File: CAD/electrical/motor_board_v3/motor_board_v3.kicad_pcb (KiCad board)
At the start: 4 copper layers, 62 x 34 mm, 82 parts, among them J1 Conn_ST_STDC14, J2 12V, J3 I2C, J4 RS485, J5 Stepper, J6 Stepper, J7 Stepper, Q1 SI2301CDS-T1-GE3, U1 STM32F401RCTx, U2 MAX485E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

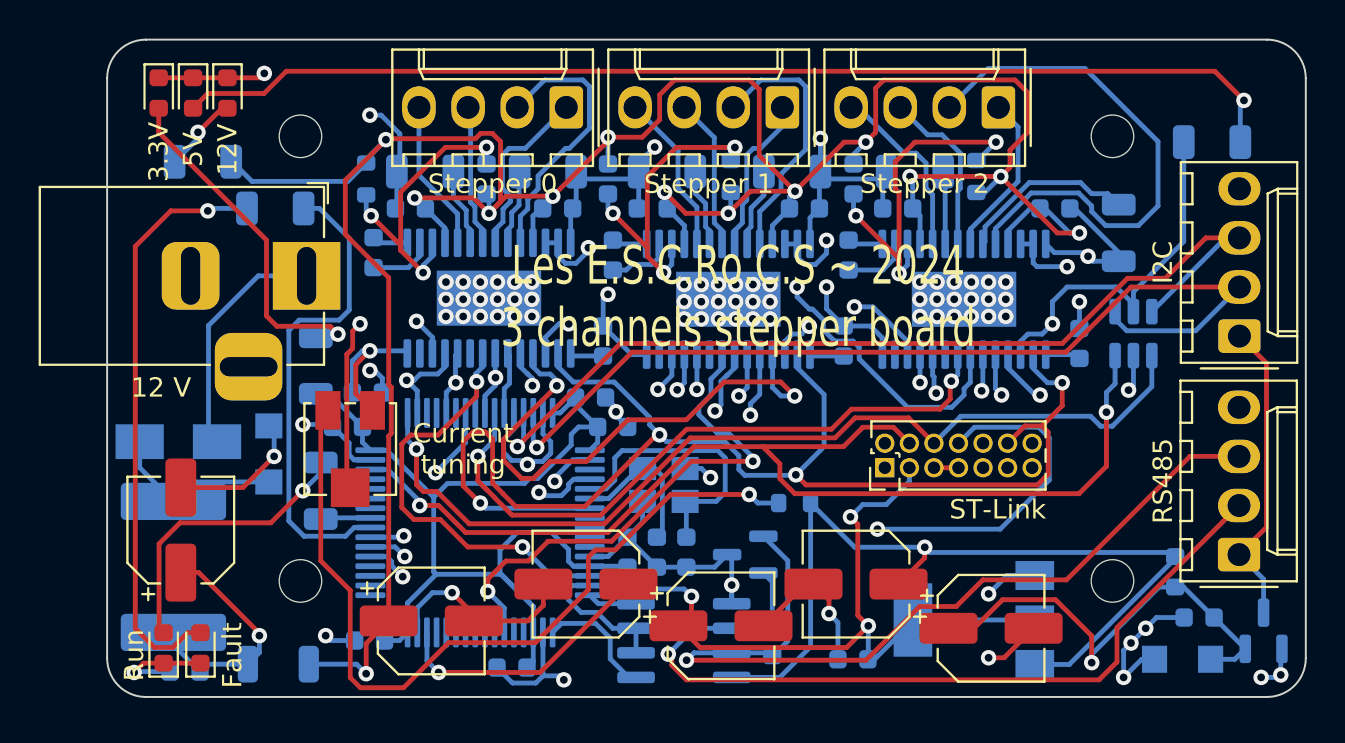
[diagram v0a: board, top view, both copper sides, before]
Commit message: Updated version of motor board and main board (#3)
* Cleaning backup files

* [WIP] Main board V2

* [WIP] Implement RS485 in ultrasonic board

* Updated version of motor board and main board
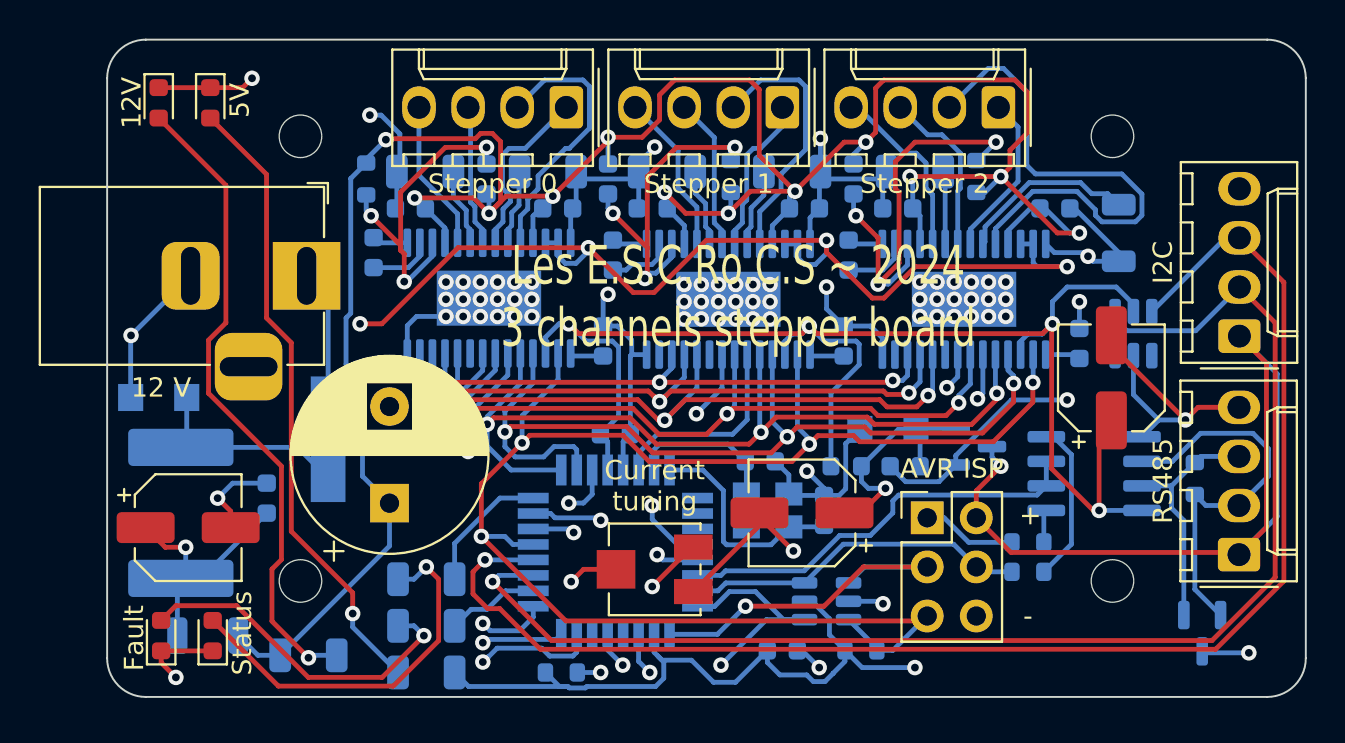
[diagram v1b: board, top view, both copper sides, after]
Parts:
- removed C23, C25, C26, C27, C28, C33: 100n, Capacitor_SMD:C_0603_1608Metric
- removed C29: 4.7u, Capacitor_SMD:CP_Elec_5x5.4
- removed C32: 10u, Capacitor_SMD:CP_Elec_5x5.4
- removed D4: 3V3, LED_SMD:LED_0603_1608Metric
- removed R8: 470, Resistor_SMD:R_1206_3216Metric
- added R19: 10k, Resistor_SMD:R_0603_1608Metric, B.Cu at (170.6, 110.7)
- added R2: 330, Resistor_SMD:R_0603_1608Metric, B.Cu at (179.2, 106.7)
- added R3: 330, Resistor_SMD:R_0603_1608Metric, B.Cu at (179.2, 105.2)
- C1, C2: value 22p -> 100n
- C11, C17: value 100n -> 22p
- C30: footprint Capacitor_SMD:CP_Elec_5x5.4 -> Capacitor_THT:CP_Radial_D10.0mm_P5.00mm
- J1: value Conn_ST_STDC14 -> AVR-ISP-6; footprint Connector_PinHeader_1.27mm:PinHeader_2x07_P1.27mm_Vertical -> Connector_PinHeader_2.54mm:PinHeader_2x03_P2.54mm_Vertical
- U1: value STM32F401RCTx -> ATmega328PB-A; footprint Package_QFP:LQFP-64_10x10mm_P0.5mm -> Package_QFP:TQFP-32_7x7mm_P0.8mm
- U6: value AMS1117-3.3 -> SRV05-4; footprint Package_TO_SOT_SMD:SOT-223-3_TabPin2 -> Package_TO_SOT_SMD:SOT-23-6
- Y1: value 25MHz -> 16MHz
- moved R7 49.0 mm to (148.1, 111.9), turned to 180 degrees
- moved R1 26.1 mm to (142.0, 111.0), turned to 0 degrees
- moved D9 24.0 mm to (188.2, 109.9), turned to -90 degrees
- moved R5 23.4 mm to (187.8, 101.9), turned to -90 degrees
- moved R4 23.0 mm to (148.1, 109.5)
- moved U2 22.9 mm to (182.6, 101.6)
- moved C11 20.6 mm to (165.4, 101.0), turned to 0 degrees
- moved D7 19.3 mm to (172.0, 99.3)
- moved FB2 17.9 mm to (169.8, 101.2), turned to 180 degrees
- moved Q1 17.8 mm to (176.4, 100.2), turned to 0 degrees
- moved C4 17.1 mm to (172.8, 101.2)
- moved C31 17.0 mm to (183.5, 96.6), turned to 90 degrees
- moved RV1 16.9 mm to (159.9, 106.6), turned to -90 degrees
- moved R18 14.9 mm to (155.1, 111.9), turned to 0 degrees
- moved C3 11.5 mm to (167.5, 103.6), turned to 180 degrees
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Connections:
- C1 pad 1: /XTAL1 -> +5V
- C11 pad 1: /RST -> /XTAL1
- C17 pad 1: +3V3 -> /XTAL2
- C2 pad 1: /XTAL2 -> +5V
- J1 pad 1: unconnected-(J1-Pad1) -> /SPI_MISO
- J1 pad 2: unconnected-(J1-Pad2) -> /RAW_5V
- J1 pad 3: +3V3 -> /SPI_SCK
- J1 pad 4: /SWDIO -> /SPI_MOSI
- J1 pad 5: GND -> /RST
- J1 pad 6: /SWCLK -> GND
- U1 pad 1: +3V3 -> /DECAY
- U1 pad 12: GND -> /STEP_EN
- U1 pad 13: +3V3 -> /STEP0
- U1 pad 14: /STEP0 -> /RS485_TXE
- U1 pad 15: /RS485_TXE -> /SPI_MOSI
- U1 pad 16: /UART_TXD -> /SPI_MISO
- U1 pad 17: /UART_RXD -> /SPI_SCK
- U1 pad 18: GND -> +5V
- U1 pad 19: +3V3 -> /DIR2
- U1 pad 2: /DIR1 -> /FAULT
- U1 pad 21: unconnected-(U1-Pad21) -> GND
- U1 pad 22: /STEP1 -> unconnected-(U1-Pad22)
- U1 pad 23: unconnected-(U1-Pad23) -> /MODE0
- U1 pad 24: unconnected-(U1-Pad24) -> /MODE1
- U1 pad 25: unconnected-(U1-Pad25) -> /MODE2
- U1 pad 26: unconnected-(U1-Pad26) -> /FAULT_ST
- U1 pad 27: unconnected-(U1-Pad27) -> /I2C_SDA
- U1 pad 28: unconnected-(U1-Pad28) -> /I2C_SCL
- U1 pad 29: unconnected-(U1-Pad29) -> /RST
- U1 pad 3: unconnected-(U1-Pad3) -> /DIR0
- U1 pad 30: Net-(C29-Pad1) -> /STEP1
- U1 pad 31: GND -> /STEP2
- U1 pad 32: +3V3 -> /STATUS
- U1 pad 4: /DECAY -> +5V
- U1 pad 5: /XTAL1 -> GND
- U1 pad 6: /XTAL2 -> /DIR1
- U1 pad 7: /RST -> /XTAL1
- U1 pad 8: unconnected-(U1-Pad8) -> /XTAL2
- U6 pad 1: GND -> /SPI_SCK
- U6 pad 2: +3V3 -> GND
- U6 pad 3: +5V -> /RST
- U8 pad 1: /SWCLK -> unconnected-(U8-Pad1)
- U8 pad 3: /SWDIO -> unconnected-(U8-Pad3)
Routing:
- net +3V3: track 91.1 -> 0.00 mm, vias 3 -> 0
- net /SWDIO: track 57.7 -> 0.00 mm, vias 2 -> 0
- net /SWO: track 54.8 -> 0.00 mm, vias 2 -> 0
- net /SWCLK: track 48.8 -> 0.00 mm, vias 1 -> 0
- net /MODE0: track 37.2 -> 71.1 mm, vias 3 -> 4
- net Net-(R18-Pad2): track 41.8 -> 9.64 mm, vias 1 -> 2
- net /RS485_A: track 44.4 -> 12.6 mm, vias 1 -> 0
- net /SPI_MISO: track 0.00 -> 30.5 mm, vias 0 -> 1
- net Net-(D8-Pad2): track 3.78 -> 33.8 mm
- net /RAW_5V: track 16.0 -> 44.0 mm, vias 0 -> 1
- net Net-(D3-Pad2): track 58.0 -> 32.7 mm
- net /I2C_SCL: track 49.1 -> 73.2 mm
- net /RS485_B: track 43.7 -> 20.4 mm, vias 1 -> 0
- net /MODE1: track 40.2 -> 61.0 mm, vias 3 -> 4
- net /FAULT_ST: track 24.9 -> 4.82 mm
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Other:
- board text added: "+"
- board text added: "-"
- board text added: "AVR ISP"
- board text added: "Status"
- board text removed: "3.3V"
- board text removed: "Run"
- board text removed: "ST-Link"
